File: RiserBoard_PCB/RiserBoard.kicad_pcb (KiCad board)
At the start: 2 copper layers, 35.6 x 14 mm, 11 parts, among them J1 BUS1, J2 Input, J3 BUS2

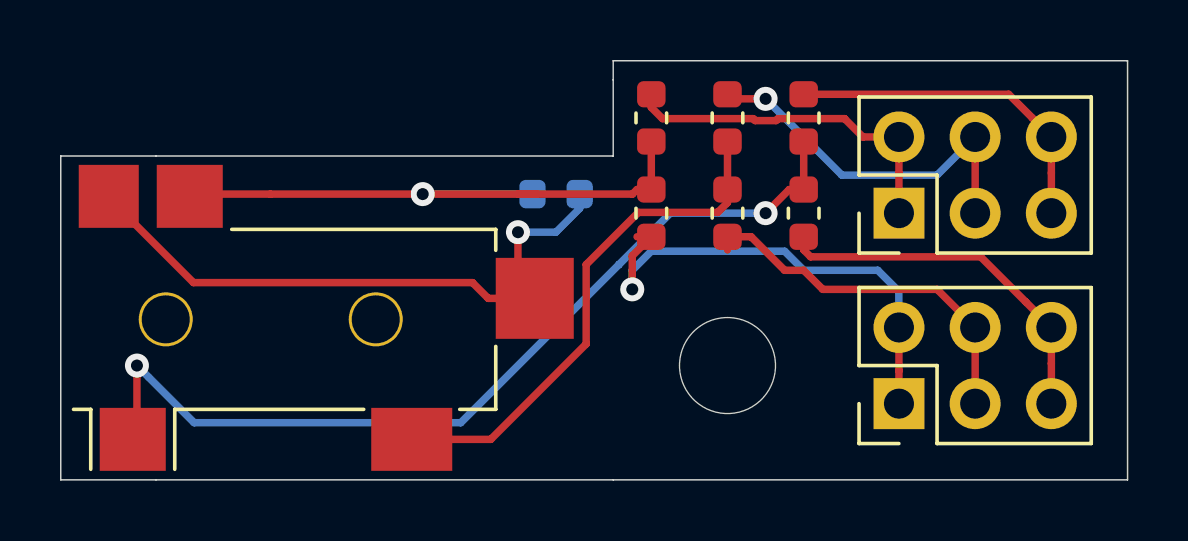
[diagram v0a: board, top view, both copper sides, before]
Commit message: Updated Design to v0.1
Smaller PCB
Only 1 sided PCB
Different Jack Footprint
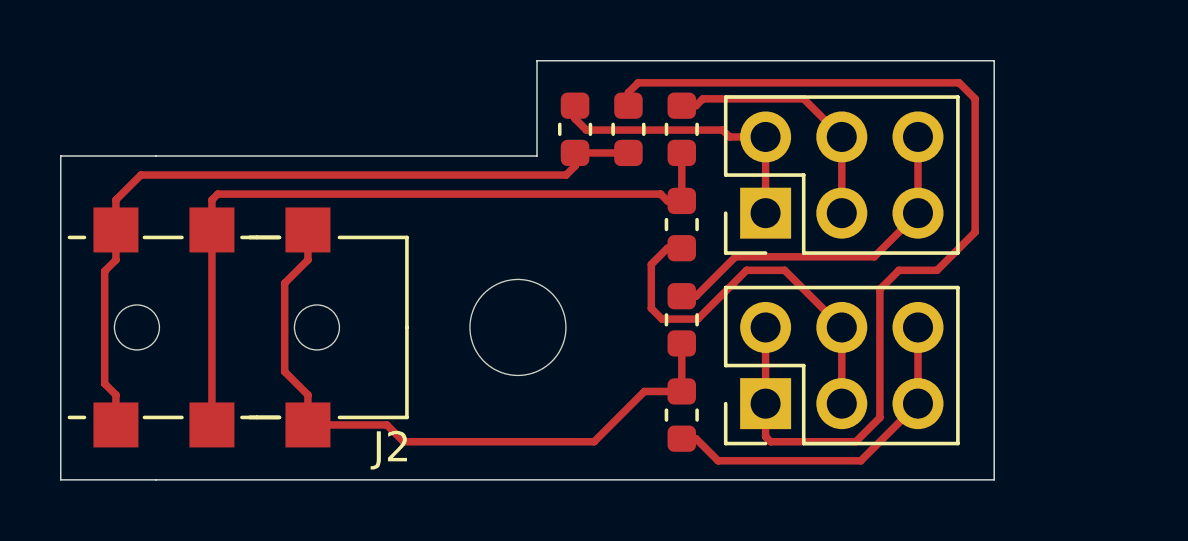
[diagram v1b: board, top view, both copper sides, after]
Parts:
- removed R1: 10K, Resistor_SMD:R_0603_1608Metric
- J2: value Input -> AudioJack3; footprint Jack_3.5mm_Switchcraft_35RASMT4BHNTRX:Jack_3.5mm_Switchcraft_35RASMT4BHNTRX -> Jack_3.5mm_PJ-313D-6A:PJ-313D-6A
- JP1: value G_1 -> G_T
- JP2: value G_2 -> G_B
- JP3: value L_1 -> L_T
- JP4: value L_2 -> L_B
- JP5: value R_1 -> R_T
- JP6: value R_2 -> R_B
- moved H1 7.10 mm to (141.6, 92.1)
- moved JP3 6.90 mm to (147.1, 95.0)
- moved JP4 6.90 mm to (147.1, 91.8)
- moved J1 4.44 mm to (149.9, 94.6)
- moved J3 4.44 mm to (149.9, 88.3)
- moved JP5 4.08 mm to (147.1, 88.6)
- moved JP6 4.08 mm to (147.1, 85.5)
- moved J2 3.73 mm to (128.9, 92.1), turned to 90 degrees
- moved JP1 2.90 mm to (145.3, 85.5), turned to 270 degrees
- moved JP2 2.57 mm to (143.5, 85.5)
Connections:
- net /1_GND renamed /T_S
- net /2_GND renamed /B_S
- J1 pad 3: /1_L -> /T_R
- J1 pad 4: /1_L -> /T_R
- J1 pad 5: /1_R -> /T_L
- J1 pad 6: /1_R -> /T_L
- J3 pad 3: /2_L -> /B_R
- J3 pad 4: /2_L -> /B_R
- J3 pad 5: /2_R -> /B_L
- J3 pad 6: /2_R -> /B_L
- JP3 pad 1: /1_L -> /T_L
- JP4 pad 2: /2_L -> /B_L
- JP5 pad 1: /1_R -> /T_R
- JP6 pad 2: /2_R -> /B_R
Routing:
- net Net-(J2-PadRN): track 21.8 -> 0.00 mm, vias 1 -> 0
- net /T_S: track 16.6 -> 32.9 mm, vias 1 -> 0
- net /T_R: track 0.00 -> 13.2 mm
- net /1_L: track 12.5 -> 0.00 mm
- net /2_L: track 12.4 -> 0.00 mm, vias 1 -> 0
- net /1_R: track 12.3 -> 0.00 mm
- net /B_L: track 0.00 -> 11.6 mm
- net /T_L: track 0.00 -> 11.5 mm
- net /2_R: track 11.4 -> 0.00 mm
- net /B_R: track 0.00 -> 8.49 mm
- net Net-(J2-PadR): track 30.4 -> 24.9 mm, vias 2 -> 0
- net Net-(J2-PadT): track 17.4 -> 22.1 mm
- net Net-(J2-PadS): track 21.4 -> 25.8 mm, vias 1 -> 0
- net /B_S: track 11.7 -> 9.58 mm
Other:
- board size 35.6 x 14 mm -> 31.1 x 14 mm
- board text added: "3.5mm RiserBoard"
- board text added: "v0.1"
- board text removed: "3.5 RiserBoard"
- board text removed: "v0.0"
